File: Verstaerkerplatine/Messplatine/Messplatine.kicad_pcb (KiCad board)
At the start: 2 copper layers, 99.1 x 99.1 mm, 48 parts, among them J1 Conn_01x20_Socket, J14 Conn_01x20_Socket, J26 Conn_02x20_Odd_Even, U1 MCP6042, U10 KY-051, U11 ULN2003, U3 TMA0505D, U31 Powersupply, U4 CA3140, U5 AD623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

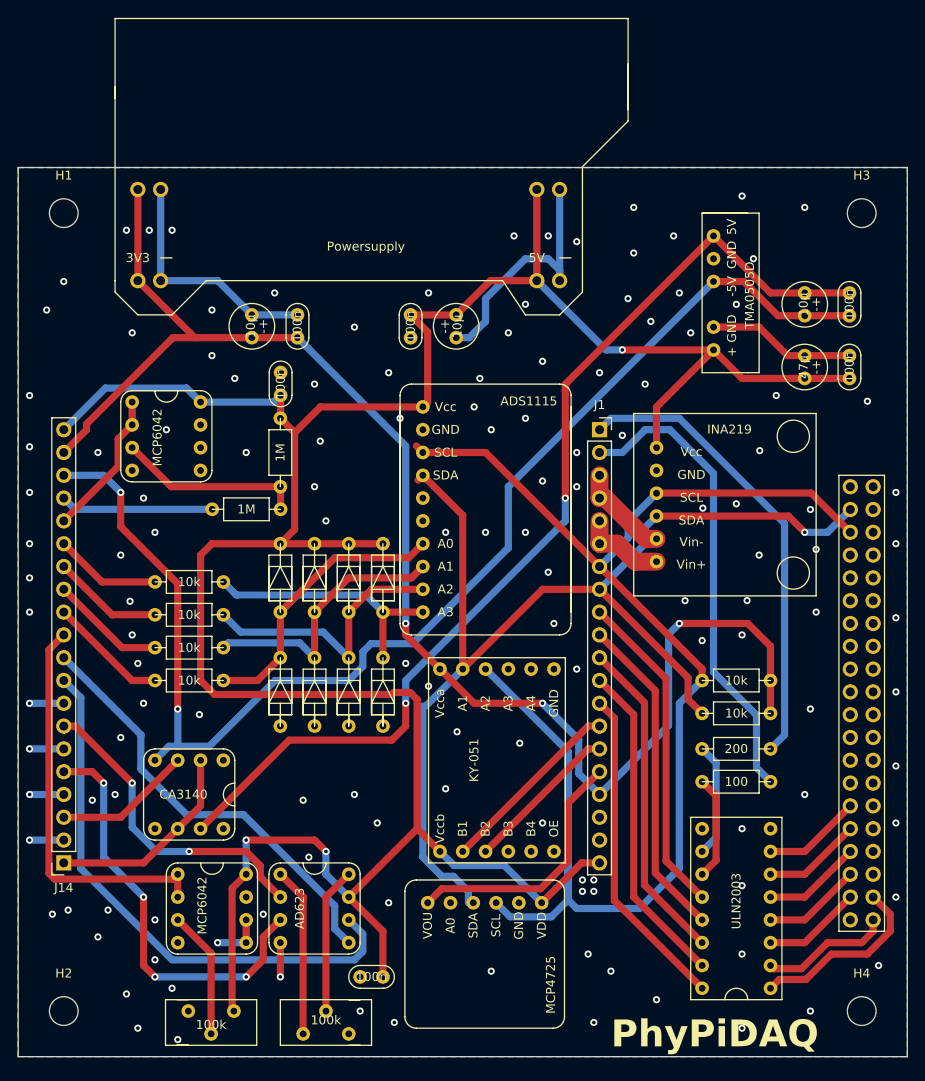
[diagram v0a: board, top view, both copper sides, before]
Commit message: added Jumpers for 3.3V and 5V from Raspberry Pi
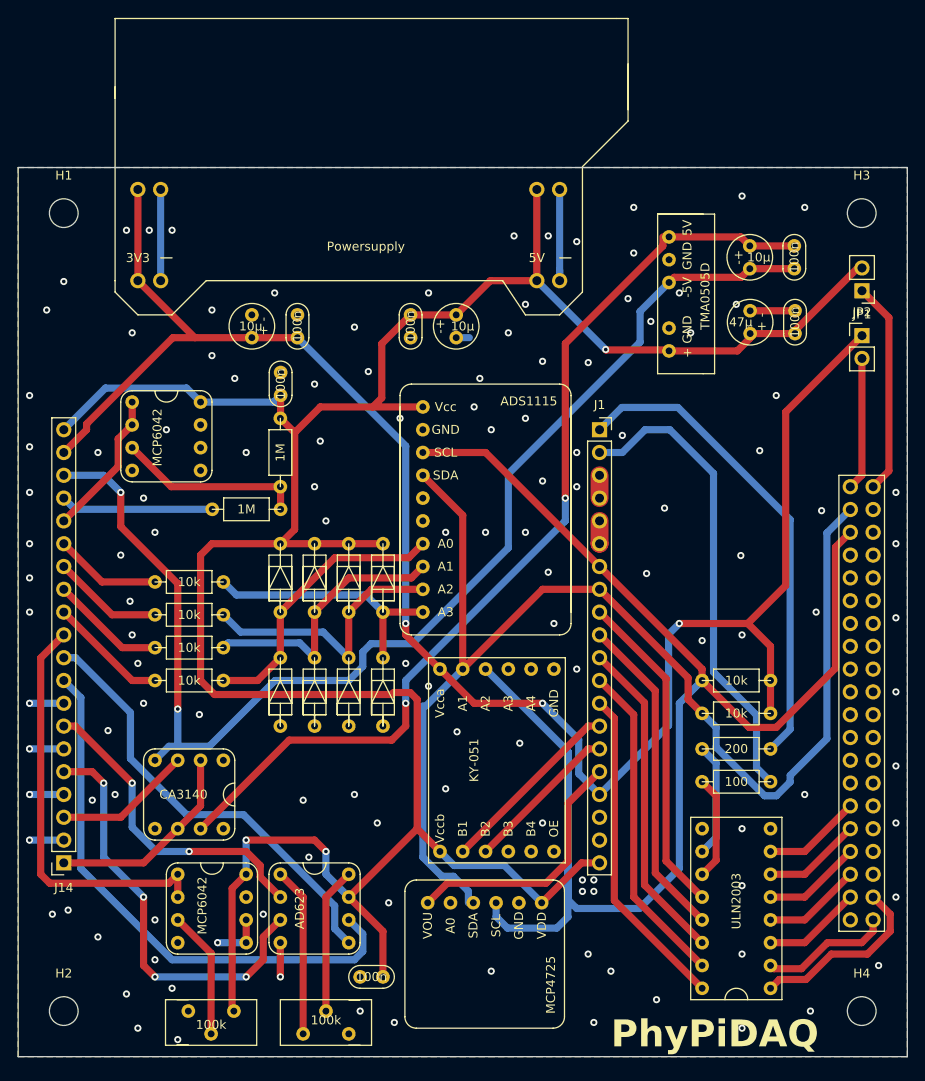
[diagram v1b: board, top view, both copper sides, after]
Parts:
- removed U6: INA219, LibraryPhyPiDAQ:INA219
- added JP1: +3.3V, Connector_PinHeader_2.54mm:PinHeader_1x02_P2.54mm_Vertical, F.Cu at (204.5, 83.5)
- added JP2: +5V, Connector_PinHeader_2.54mm:PinHeader_1x02_P2.54mm_Vertical, F.Cu at (204.5, 78.5)
- moved C9 8.08 mm to (199.5, 74.8)
- moved C3 7.87 mm to (189.5, 82.0)
- moved C1 7.86 mm to (194.5, 82.0)
- moved C10 5.34 mm to (194.5, 74.8), turned to -90 degrees
- moved U3 4.96 mm to (180.5, 80.1)
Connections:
- C10 pad 1: -5V -> Net-(U4-V+)
- C10 pad 2: Net-(U4-V+) -> -5V
- J26 pad 1: unconnected-(J26-Pin_1-Pad1) -> Net-(J26-Pin_1)
- J26 pad 2: unconnected-(J26-Pin_2-Pad2) -> Net-(J26-Pin_2)
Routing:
- net GND: track 96.7 -> 53.1 mm, vias 138 -> 129
- net +3.3V: track 161.6 -> 198.9 mm
- net Net-(J26-Pin_2): track 0.00 -> 23.8 mm
- net Net-(J26-Pin_1): track 0.00 -> 14.8 mm
- net SDA_3.3: track 126.6 -> 140.4 mm, vias 1 -> 0
- net StromSpannungsSensor_IN_-: track 10.8 -> 2.54 mm
- net +5V: track 306.9 -> 298.9 mm
- net StromSpannungsSensor_IN_+: track 9.72 -> 2.54 mm
- net Net-(U4-V+): track 114.2 -> 108.3 mm
- net -5V: track 144.0 -> 139.8 mm
- net SCL_3.3: track 169.8 -> 173.1 mm
- net LED1: track 51.7 -> 53.9 mm
- net Referenzspannung_OUT: track 44.6 -> 46.4 mm
- net Instrumentenverstaerker_Ref: track 48.6 -> 49.4 mm

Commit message: introduced direct wire connections for CA3160 and INA219
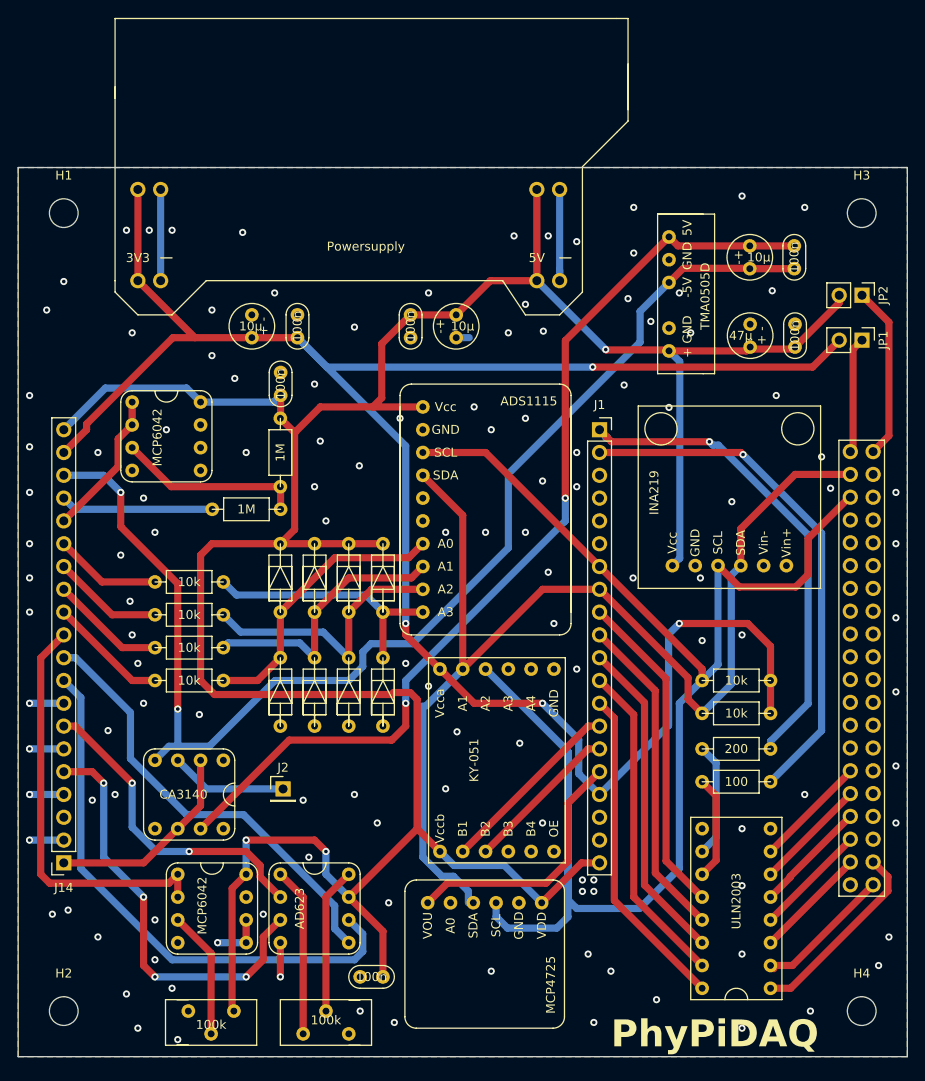
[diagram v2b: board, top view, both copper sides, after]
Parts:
- added J2: Elektrometer_In, Connector_PinHeader_2.54mm:PinHeader_1x01_P2.54mm_Vertical, F.Cu at (140.0, 134.0)
- added U6: INA219, LibraryPhyPiDAQ:INA219, F.Cu at (178.3, 104.0)
- JP1: value +3.3V -> J_2_Open
- JP2: value +5V -> J_2_Open
- moved J26 3.91 mm to (205.7, 93.9)
- moved C1 1.50 mm to (194.5, 83.5)
- moved C3 1.50 mm to (189.5, 83.5)
- moved JP1 0.50 mm to (204.5, 84.0), turned to -90 degrees
- moved JP2 0.50 mm to (204.5, 79.0), turned to -90 degrees
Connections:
- J1 pad 3: StromSpannungsSensor_IN_- -> unconnected-(J1-Pin_3-Pad3)
- J1 pad 4: StromSpannungsSensor_IN_- -> unconnected-(J1-Pin_4-Pad4)
- J1 pad 5: StromSpannungsSensor_IN_+ -> unconnected-(J1-Pin_5-Pad5)
- J1 pad 6: StromSpannungsSensor_IN_+ -> unconnected-(J1-Pin_6-Pad6)
- J14 pad 3: Elektrometer_IN_+ -> GND
- JP1 pad 1: +3.3V -> Net-(J26-Pin_1)
- JP1 pad 2: Net-(J26-Pin_1) -> +3.3V
- U4 pad 3: Elektrometer_IN_+ -> Net-(J2-Pin_1)
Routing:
- net +3.3V: track 198.9 -> 224.6 mm, vias 3 -> 4
- net +5V: track 298.9 -> 319.7 mm
- net Elektrometer_IN_+: track 15.3 -> 0.00 mm
- net Net-(J2-Pin_1): track 0.00 -> 13.1 mm
- net SDA_3.3: track 140.4 -> 128.8 mm
- net LED2: track 52.7 -> 58.5 mm, vias 0 -> 1
- net GND: track 53.1 -> 47.8 mm, vias 129 -> 128
- net Net-(J26-Pin_2): track 23.8 -> 19.4 mm
- net StromSpannungsSensor_IN_-: track 2.54 -> 0.00 mm
- net StromSpannungsSensor_IN_+: track 2.54 -> 0.00 mm
- net Net-(J26-Pin_37): track 11.0 -> 12.7 mm
- net Net-(J26-Pin_33): track 11.0 -> 12.7 mm
- net Net-(J26-Pin_29): track 11.0 -> 12.7 mm
- net Net-(J26-Pin_35): track 11.0 -> 12.7 mm
- net Net-(J26-Pin_31): track 11.0 -> 12.7 mm
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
